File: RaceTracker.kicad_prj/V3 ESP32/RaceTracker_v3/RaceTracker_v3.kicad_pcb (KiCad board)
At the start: 4 copper layers, 49 x 58.5 mm, 45 parts, among them J1 USB-C, J2 Battery, J3 Qwiic GPS (I2C), J4 microSD, J5 UART Debug, J6 e-Paper (steckbar) 8p, SW1 PWR, SW2 RESET, SW3 BOOT, U1 ESP32-S3-WROOM-1-N8, U2 MCP73831T-2ACI/OT, U3 AP2112K-3.3, U4 WSEN-ISDS

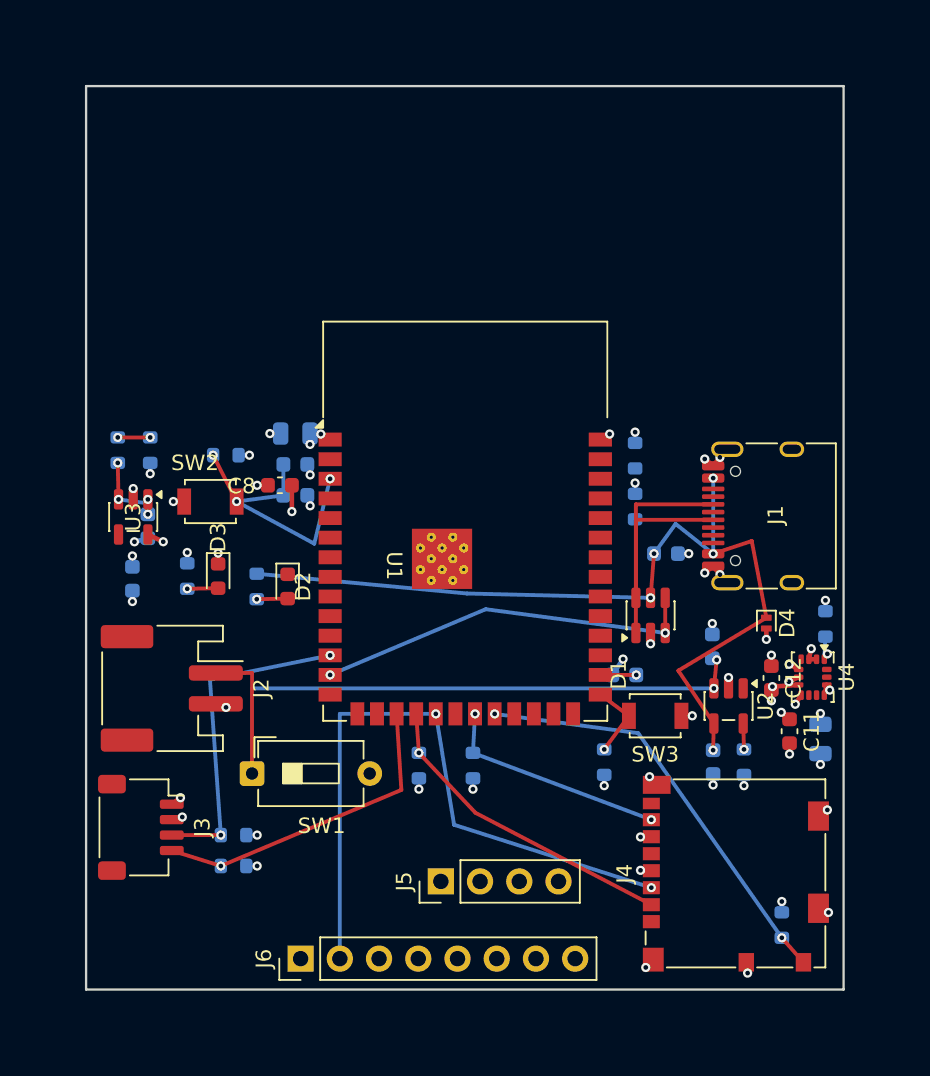
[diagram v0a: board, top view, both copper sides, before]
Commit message: V3: alle Traces entfernt, GND/+3V3-Plane-Vias behalten
Vorbereitung fuer manuelles Neu-Routing mit runden Leiterbahnen.

- 123 PCB_TRACK geloescht (alle Netze)
- 34 Signal-/Power-Vias geloescht (+VBUS, +VBAT_*, USB, SD, I2C, ...)
- 62 Vias behalten: 41x /GND (In1.Cu-Plane), 21x /+3V3 (In2.Cu-Plane)
- Zonen In1.Cu/In2.Cu neu gefuellt
- Footprint-Platzierung unveraendert (45 Footprints)

Backup der Vorversion: siehe Commit acf4591.

Co-Authored-By: Claude Opus 5 (1M context) <noreply@anthropic.com>
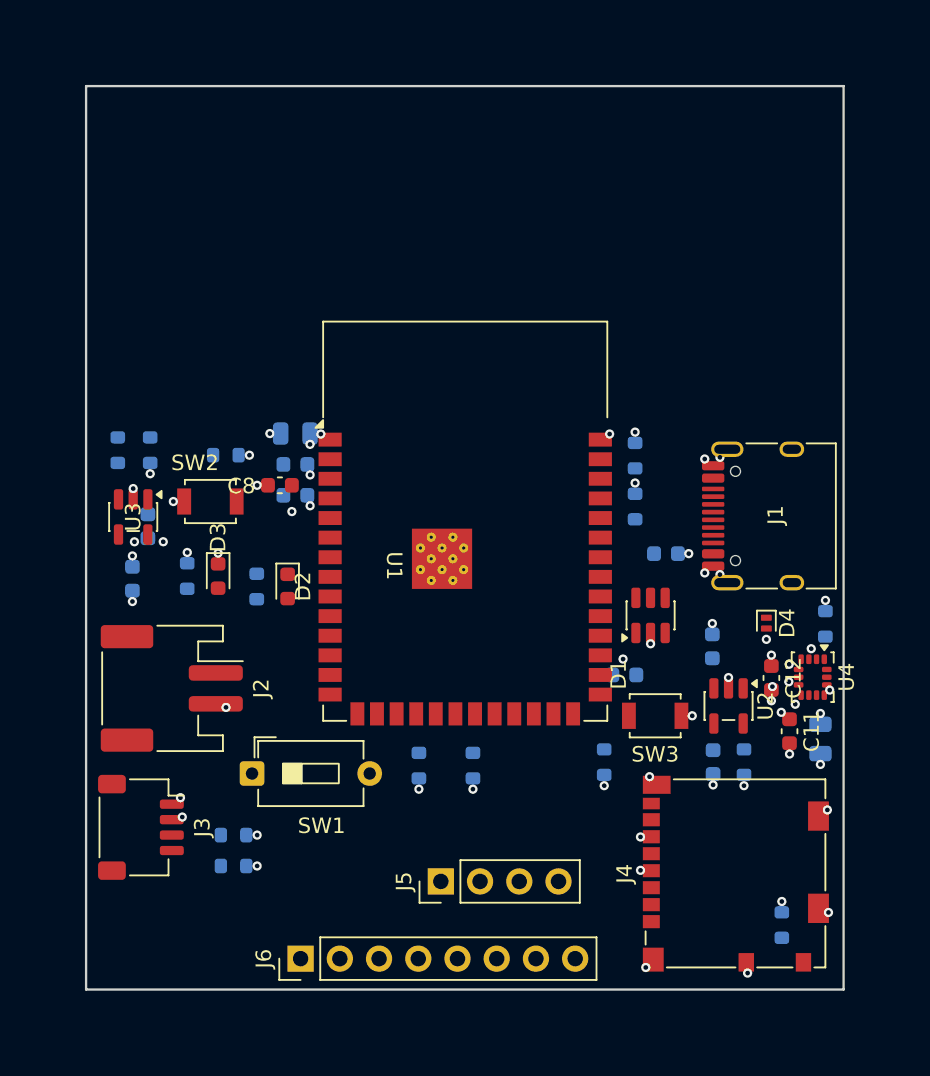
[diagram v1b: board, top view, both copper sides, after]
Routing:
- net /+VBUS: track 59.0 -> 0.00 mm, vias 5 -> 0
- net /+VBAT_RAW: track 46.1 -> 0.00 mm, vias 2 -> 0
- net /SD_MOSI: track 42.7 -> 0.00 mm, vias 2 -> 0
- net /GND: track 30.4 -> 0.00 mm
- net /SD_CD: track 27.7 -> 0.00 mm, vias 2 -> 0
- net /USB_DM: track 24.9 -> 0.00 mm, vias 2 -> 0
- net /USB_DP: track 23.4 -> 0.00 mm
- net /I2C_SDA: track 21.2 -> 0.00 mm, vias 2 -> 0
- net /I2C_SCL: track 20.9 -> 0.00 mm, vias 1 -> 0
- net /SD_CS: track 20.7 -> 0.00 mm, vias 1 -> 0
- net Net-(U1-EN): track 18.5 -> 0.00 mm, vias 3 -> 0
- net /+3V3: track 17.0 -> 0.00 mm
- net /SD_MISO: track 14.9 -> 0.00 mm, vias 2 -> 0
- net /+VBAT_SYS: track 5.52 -> 0.00 mm, vias 4 -> 0
- net Net-(U1-IO0): track 5.01 -> 0.00 mm, vias 1 -> 0
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
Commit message: V3: alle DRC-Errors und Silk-Warnungen behoben (0/0)
Nach dem manuellen Routing des Users durch den User:

Elektrische Fehler (kicad-cli DRC: 67 Violations, 14 offene Verbindungen -> 0/0):
- Kurzschluss BATT_SENSE/GND behoben: Track um GND-Stitching-Via (78.0,66.5)
  herum verlegt, Via selbst nach (78.6,66.63) verschoben + Steg zu C6.2 ergaenzt
  (Pad U1.28 lag zu nah am urspruenglichen Via-Standort)
- 21 redundante/doppelte/schwebende Vias entfernt (10 exakte Duplikate,
  3 ueberfluessig neben PTH-Pads, 6 nutzlos auf SMD-Pads ohne Lagenwechsel,
  2 komplett freischwebend)
- 14 offene Verbindungen geschlossen: 10 verwaiste Plane-Stitching-Vias per
  kurzem Steg ans Ziel-Pad angebunden, 2 U4-Pad-Paare (GND/+3V3) direkt
  verbunden, 2 neue Vias fuer +VBAT_SYS-Lagenwechsel bei U3/C4

Silk-Warnungen (28 -> 0), nur Referenz-Textfelder angefasst, keine Bauteile
oder Traces veraendert:
- 9 Referenzen 180 Grad gespiegelt + auf 0.8mm verkleinert (freie Seite des
  eigenen Bauteils statt Ueberlappung mit Nachbarn)
- D1/U3 individuell neu positioniert nach Geometrie-Analyse
- U2/C12 Referenz ausgeblendet (keine freie Stelle im dichten Cluster
  SW3/C3/R3/C2/U4 gefunden)

Verifiziert: kicad-cli pcb drc --severity-all -> 0 violations, 0 unconnected.
kicad-cli sch erc --severity-all -> 0 violations. Alle 44 Footprints exakt
unveraendert in Position/Rotation/Seite (Diff gegen Backup).

Co-Authored-By: Claude Sonnet 5 <noreply@anthropic.com>
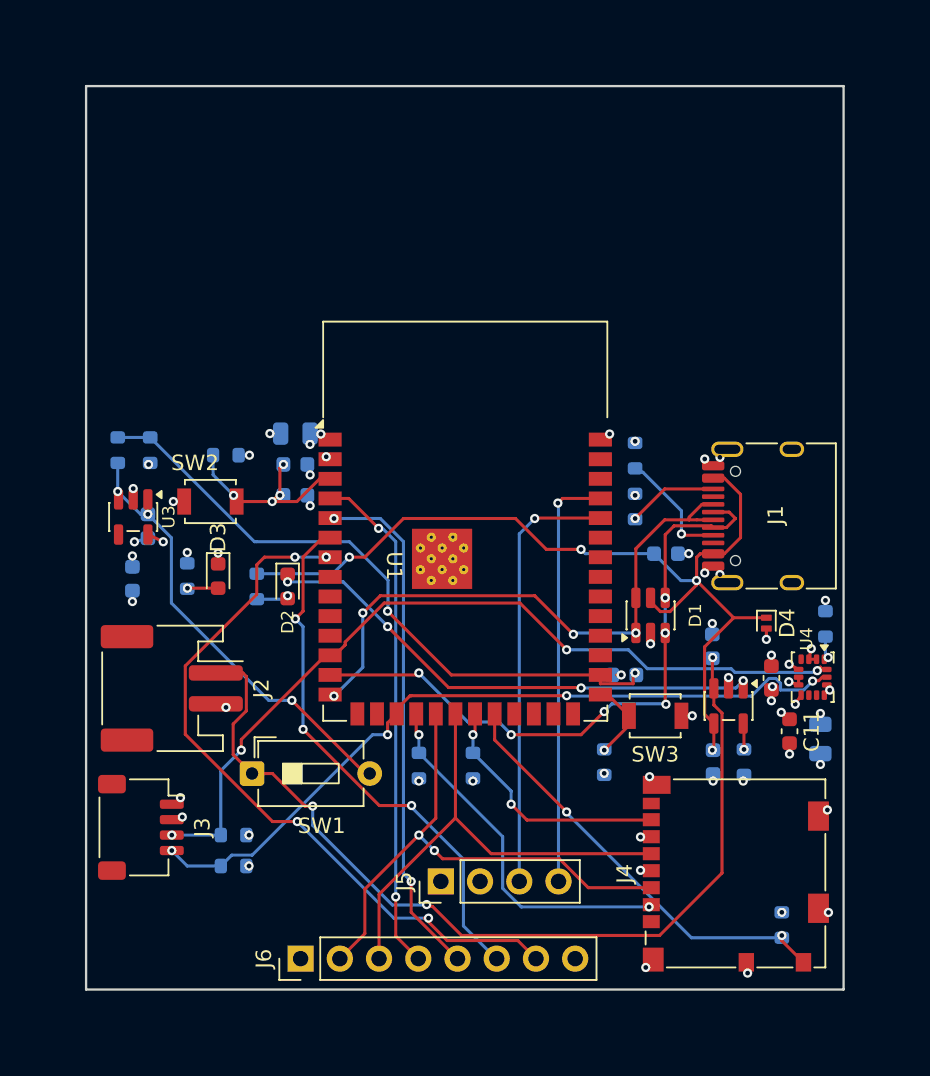
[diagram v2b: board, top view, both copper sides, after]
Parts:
- removed C8: 100nF, C_0603_1608Metric
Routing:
- net /+VBUS: track 0.00 -> 61.2 mm, vias 0 -> 4
- net /+VBAT_RAW: track 0.00 -> 60.7 mm, vias 0 -> 3
- net /I2C_SDA: track 0.00 -> 53.9 mm, vias 0 -> 4
- net /I2C_SCL: track 0.00 -> 49.5 mm, vias 0 -> 4
- net /EPD_BUSY: track 0.00 -> 46.8 mm, vias 0 -> 4
- net /BATT_SENSE: track 0.00 -> 42.6 mm, vias 0 -> 2
- net /USB_DM: track 0.00 -> 42.5 mm, vias 0 -> 6
- net /USB_DP: track 0.00 -> 38.7 mm, vias 0 -> 4
- net /EPD_RST: track 0.00 -> 35.4 mm, vias 0 -> 3
- net /SD_MOSI: track 0.00 -> 34.9 mm, vias 0 -> 2
- net /EPD_DC: track 0.00 -> 33.6 mm, vias 0 -> 2
- net /EPD_CS: track 0.00 -> 33.4 mm, vias 0 -> 2
- net /CHG_STAT: track 0.00 -> 33.1 mm, vias 0 -> 4
- net /SD_SCK: track 0.00 -> 31.5 mm
- net /+VBAT_SYS: track 0.00 -> 29.2 mm, vias 0 -> 3
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
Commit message: V3: 4 Eck-Montagebohrungen (M2, NPTH) mit Rundungs-Bossen
Board hatte bisher keine Montagebohrungen. Auf Anfrage alle 4 Ecken um
einen fast vollstaendigen Kreis (270 Grad, R=3.5mm) ergaenzt, Boss zentriert
am jeweiligen urspruenglichen Eckpunkt, Board waechst dadurch symmetrisch
um 7mm in Breite/Hoehe (49.2x58.65 -> 56.2x65.65mm), keine Bauteile
verschoben.

M2 NPTH-Bohrung (Ø2.2mm, isoliert/kein Kupfer) je Ecke:
- Board ist an den oberen Ecken (U1, nur 0.75mm Abstand) und der unteren
  rechten Ecke (J4, 0.87mm) extrem eng -> Loch-Zentrum bei 3 von 4 Ecken
  um 2.2mm diagonal nach aussen versetzt (innerhalb des 3.5mm-Boss),
  um U1s Antennen-Keepout und die Footprint-Courtyards zu clearen
- Minimales eigenes Footprint (nur NPTH-Pad + Referenztext) statt der
  KiCad-Standardbibliothek, deren eingebaute 2.45mm-Courtyard-Grafik bei
  diesem dicht gepackten Board sonst falsch-positive courtyards_overlap-
  Fehler ausgeloest haette (echte Kupfer-Clearance war nie das Problem)
- Referenztexte Richtung Board-Mitte versetzt + verkleinert, damit sie
  nicht ueber die neue gekruemmte Kante hinausragen

Verifiziert: kicad-cli pcb drc --severity-all -> 0 violations, 0
unconnected. ERC weiterhin 0/0. Alle 44 bestehenden Footprints exakt
unveraendert in Position/Rotation (Diff gegen Backup).

Co-Authored-By: Claude Sonnet 5 <noreply@anthropic.com>
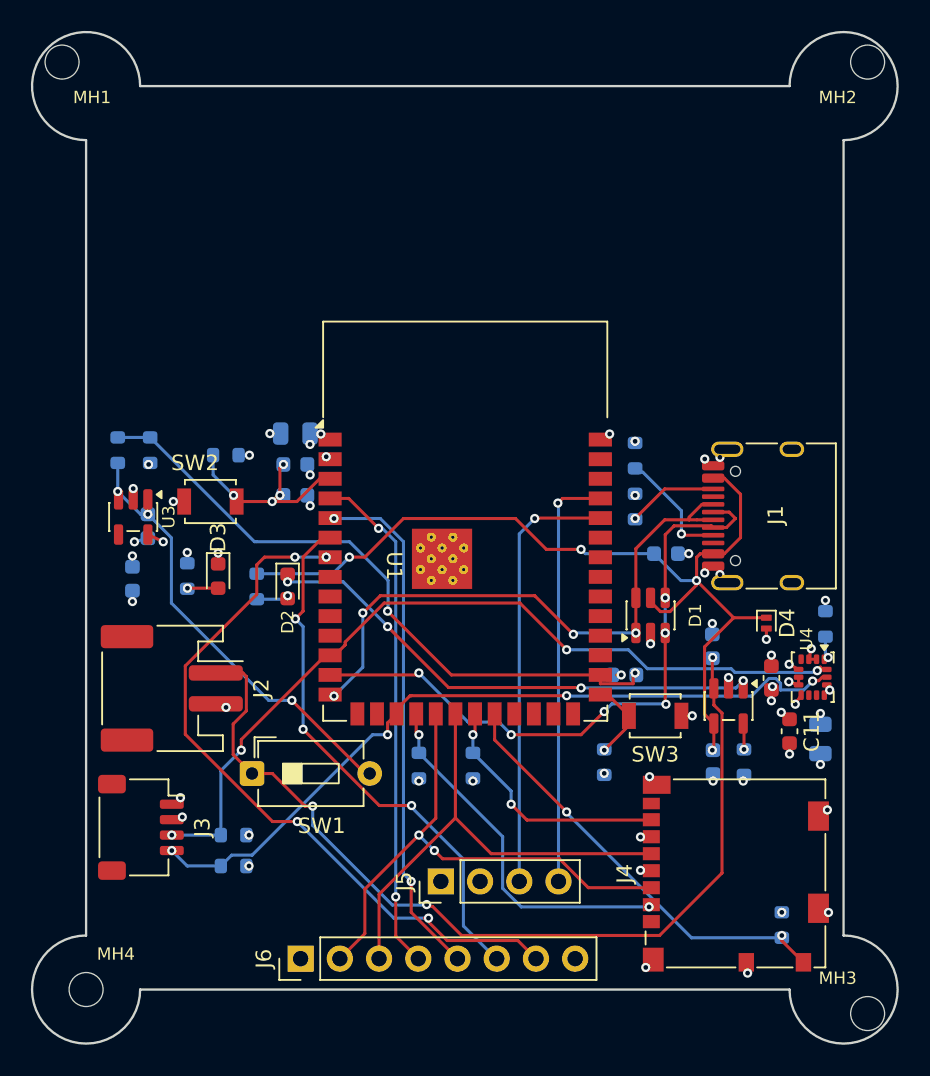
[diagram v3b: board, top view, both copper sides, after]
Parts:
- added MH1: MountingHole_2.2mm_M2, , F.Cu at (42.4, 26.9)
- added MH2: MountingHole_2.2mm_M2, , F.Cu at (94.6, 26.9)
- added MH3: MountingHole_2.2mm_M2, , F.Cu at (94.6, 88.6)
- added MH4: MountingHole_2.2mm_M2, , F.Cu at (44.0, 87.0)
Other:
- board size 49 x 58.5 mm -> 56 x 65.5 mm

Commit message: V3: Schematic-Parity-Luecken geschlossen, C8 platziert
- Alle 44 Footprint-FPIDs auf den vollen Bibliothekspfad aus dem
  Schaltplan korrigiert (waren systemweit ohne Lib-Nickname
  gespeichert, z.B. "C_0603_1608Metric" statt
  "Capacitor_SMD:C_0603_1608Metric")
- C2 Value-Feld 1uF -> 4.7uF (Schaltplan-Wert uebernommen, VBUS-Bulk-
  Cap an J1)
- U4 Datasheet- + Description-Feld aus dem Schaltplan uebernommen
- C8 (100nF, /+3V3-/GND) platziert bei (58.0,52.025)mm, F.Cu, 90 Grad
  - fehlte komplett auf der PCB, ist die fehlende HF-Entkopplung
    direkt an U1-Pin2 (3V3), analog zu C11/C12 bei U4
  - Netze zugewiesen (Ratsnest), NICHT geroutet (User routet selbst)

Verifiziert: kicad-cli pcb drc --severity-all -> 0 Errors (nur noch
5 erwartete lib_footprint_mismatch-Warnings fuer bewusst angepasste
Custom-Footprints: SW1/J6/J1/U1/J5), 1 offene Verbindung (C8,
gewollt unrouted). ERC weiterhin 0/0. Alle bestehenden Footprints
exakt unveraendert in Position (Diff-geprueft), nur C8 ist neu.

Co-Authored-By: Claude Sonnet 5 <noreply@anthropic.com>
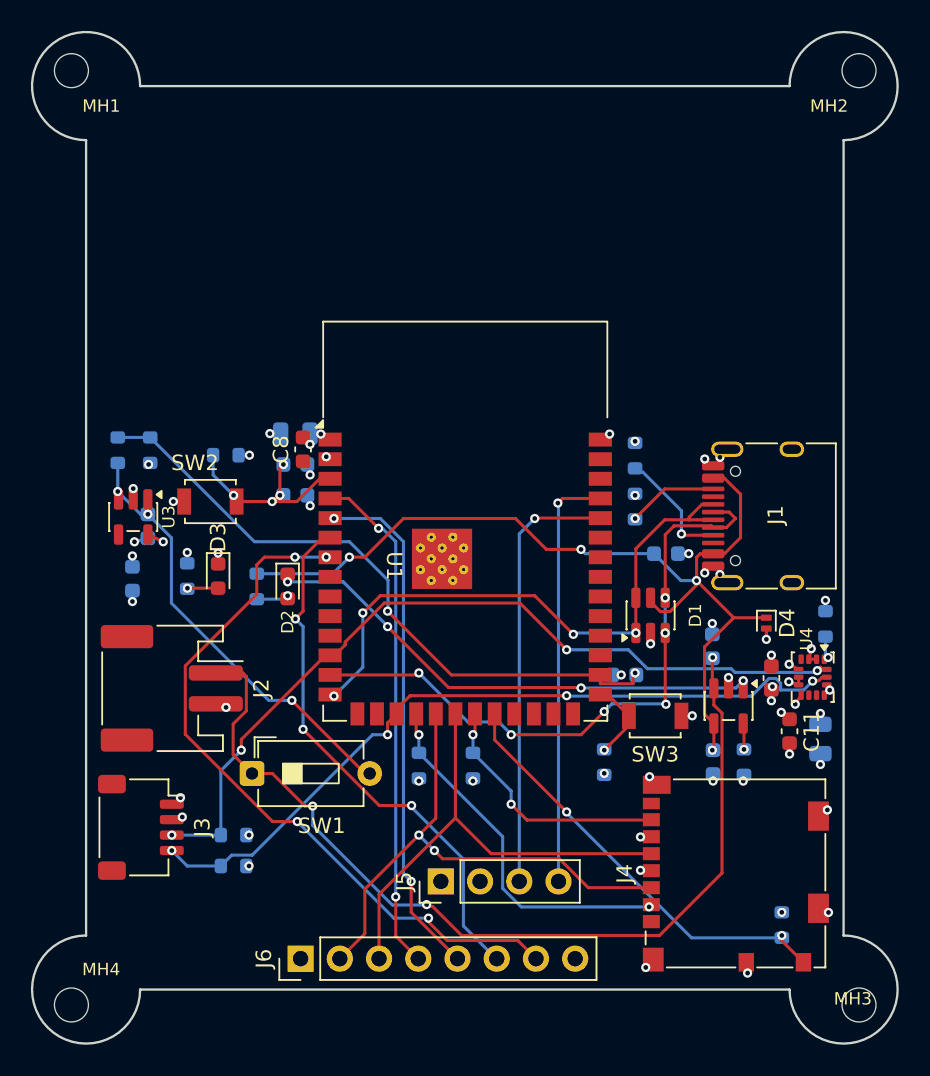
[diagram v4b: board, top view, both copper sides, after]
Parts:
- added C8: 100nF, Capacitor_SMD:C_0603_1608Metric, F.Cu at (58.0, 52.0)
- C1, C10, C11, C12, C3, C4, C5, C6, C9: footprint C_0603_1608Metric -> Capacitor_SMD:C_0603_1608Metric
- C13, C7: footprint C_0805_2012Metric -> Capacitor_SMD:C_0805_2012Metric
- C2: value 1uF -> 4.7uF; footprint C_0603_1608Metric -> Capacitor_SMD:C_0603_1608Metric
- D1: footprint SOT-23-6 -> Package_TO_SOT_SMD:SOT-23-6
- D2, D3: footprint LED_0603_1608Metric -> LED_SMD:LED_0603_1608Metric
- D4: footprint D_SOD-882 -> Diode_SMD:D_SOD-882
- J1: footprint USB_C_Receptacle_HRO_TYPE-C-31-M-12 -> Connector_USB:USB_C_Receptacle_HRO_TYPE-C-31-M-12
- J2: footprint JST_PH_S2B-PH-SM4-TB_1x02-1MP_P2.00mm_Horizontal -> Connector_JST:JST_PH_S2B-PH-SM4-TB_1x02-1MP_P2.00mm_Horizontal
- J3: footprint JST_SH_SM04B-SRSS-TB_1x04-1MP_P1.00mm_Horizontal -> Connector_JST:JST_SH_SM04B-SRSS-TB_1x04-1MP_P1.00mm_Horizontal
- J4: footprint microSD_HC_Molex_104031-0811 -> Connector_Card:microSD_HC_Molex_104031-0811
- J5: footprint PinHeader_1x04_P2.54mm_Vertical -> Connector_PinHeader_2.54mm:PinHeader_1x04_P2.54mm_Vertical
- J6: footprint PinHeader_1x08_P2.54mm_Vertical -> Connector_PinHeader_2.54mm:PinHeader_1x08_P2.54mm_Vertical
- R1, R10, R11, R12, R13, R14, R15, R2, R3, R4, R5, R6, R7, R8, R9: footprint R_0603_1608Metric -> Resistor_SMD:R_0603_1608Metric
- SW1: footprint SW_DIP_SPSTx01_Slide_6.7x4.1mm_W7.62mm_P2.54mm_LowProfile -> Button_Switch_THT:SW_DIP_SPSTx01_Slide_6.7x4.1mm_W7.62mm_P2.54mm_LowProfile
- SW2, SW3: footprint SW_SPST_B3U-1000P -> Button_Switch_SMD:SW_SPST_B3U-1000P
- U1: footprint ESP32-S3-WROOM-1 -> RF_Module:ESP32-S3-WROOM-1
- U2, U3: footprint SOT-23-5 -> Package_TO_SOT_SMD:SOT-23-5
- U4: footprint LGA-14_3x2.5mm_P0.5mm_LayoutBorder3x4y -> Package_LGA:LGA-14_3x2.5mm_P0.5mm_LayoutBorder3x4y
- moved MH4 1.38 mm to (43.0, 88.0)
- moved MH1 0.82 mm to (43.0, 27.5)
- moved MH2 0.79 mm to (94.0, 27.5)
- moved MH3 0.79 mm to (94.0, 88.0)

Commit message: V3: C8-Plane-Via, J3 zur Steckerleiste, Pin-Beschriftung
- C8: fehlenden /+3V3-Stitching-Via ergaenzt (GND-Pad hatte schon einen
  passenden Via in Reichweite, kein neuer noetig)
- J3 (Qwiic GPS I2C) von JST-SH auf 2.54mm-Stiftleiste
  (PinHeader_1x04_P2.54mm_Vertical) umgestellt - das reale SparkFun-
  Modul hat dafuer eine eigene PTH-Stiftleiste mit identischer
  Pinbelegung (GND/VCC/SDA/SCL), verifiziert gegen das Datenblatt im
  Repo-Root. Schaltplan-Footprint-Feld + PCB-Footprint getauscht,
  Position/Netze erhalten. Feinplatzierung macht der User selbst.
- Pin-Funktions-Beschriftung (Silk) fuer alle 3 Stiftleisten-Header
  J3/J5/J6 ergaenzt (GND/3V3/SDA/SCL, RXD/TXD, 3V3/MOSI/SCK/CS/DC/
  RST/BUSY/GND), 0.8mm Texthoehe, damit beim Verkabeln nichts
  vertauscht wird

Verifiziert: kicad-cli pcb drc --severity-all -> 0 Errors (nur 5
erwartete lib_footprint_mismatch-Warnings + 4 via_dangling/2
unconnected von J3s alter JST-Position, die der User beim
Neuplatzieren mit aufraeumt). ERC weiterhin 0/0.

Co-Authored-By: Claude Sonnet 5 <noreply@anthropic.com>
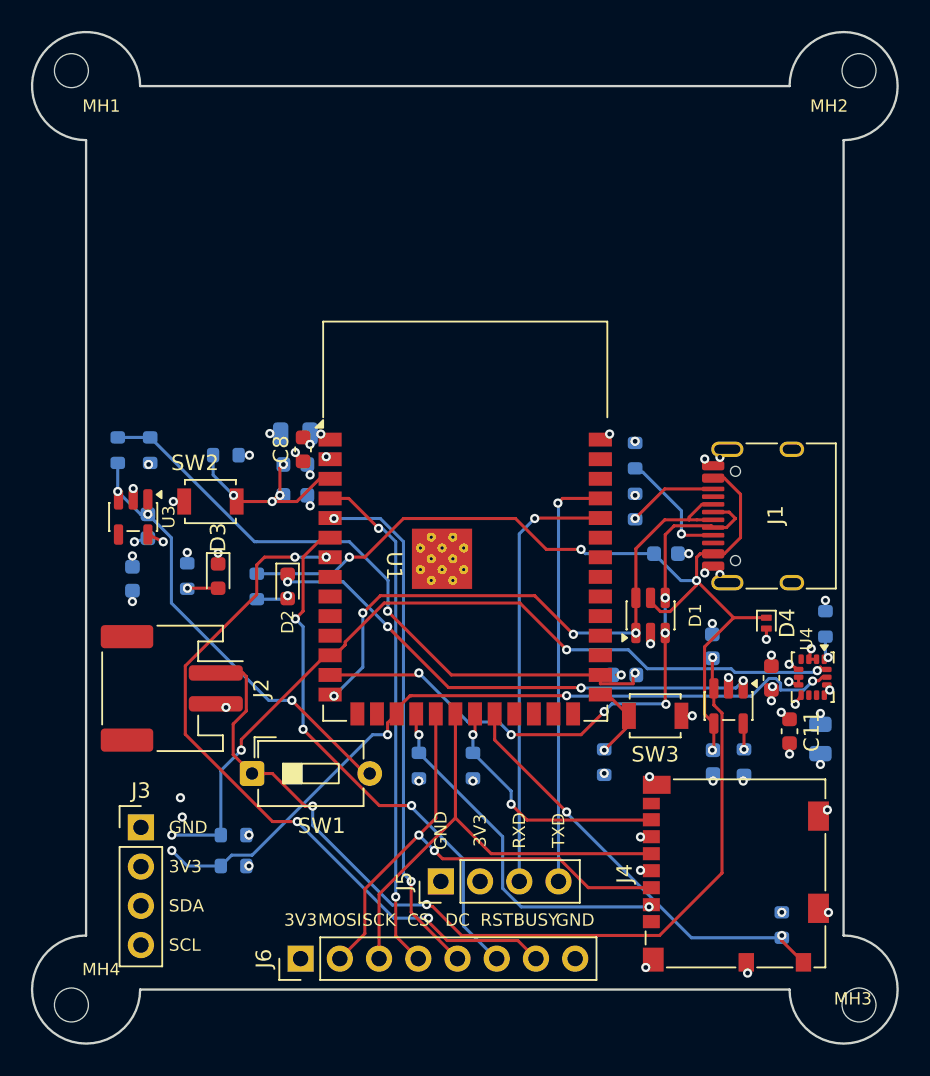
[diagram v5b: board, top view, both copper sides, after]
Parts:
- J3: footprint Connector_JST:JST_SH_SM04B-SRSS-TB_1x04-1MP_P1.00mm_Horizontal -> Connector_PinHeader_2.54mm:PinHeader_1x04_P2.54mm_Vertical
- turned J3 to 0 degrees
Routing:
- net /+3V3: vias 21 -> 22
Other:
- board text added: "3V3"
- board text added: "BUSY"
- board text added: "CS"
- board text added: "DC"
- board text added: "GND"
- board text added: "MOSI"
- board text added: "RST"
- board text added: "RXD"
- board text added: "SCK"
- board text added: "SCL"
- board text added: "SDA"
- board text added: "TXD"
